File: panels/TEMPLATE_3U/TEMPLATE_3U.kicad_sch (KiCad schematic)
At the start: 6 parts

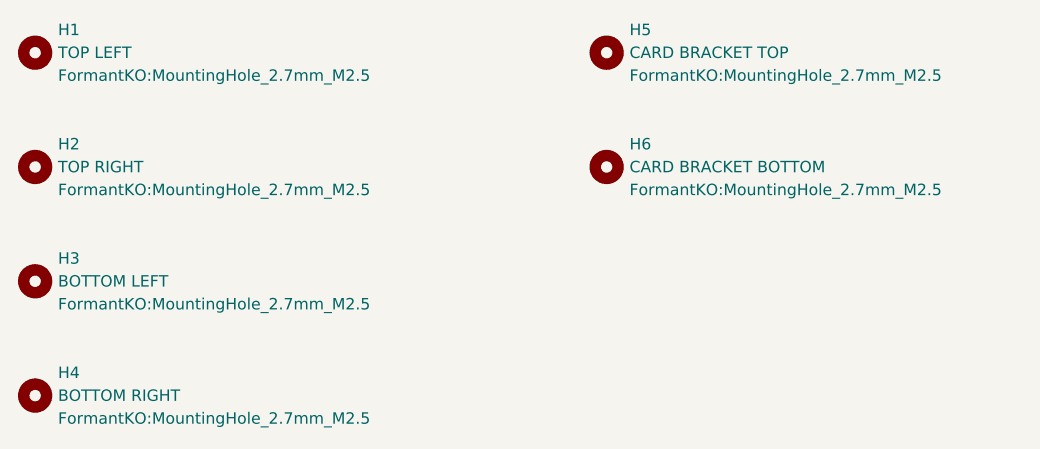
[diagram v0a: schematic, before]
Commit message: panel mounting holes
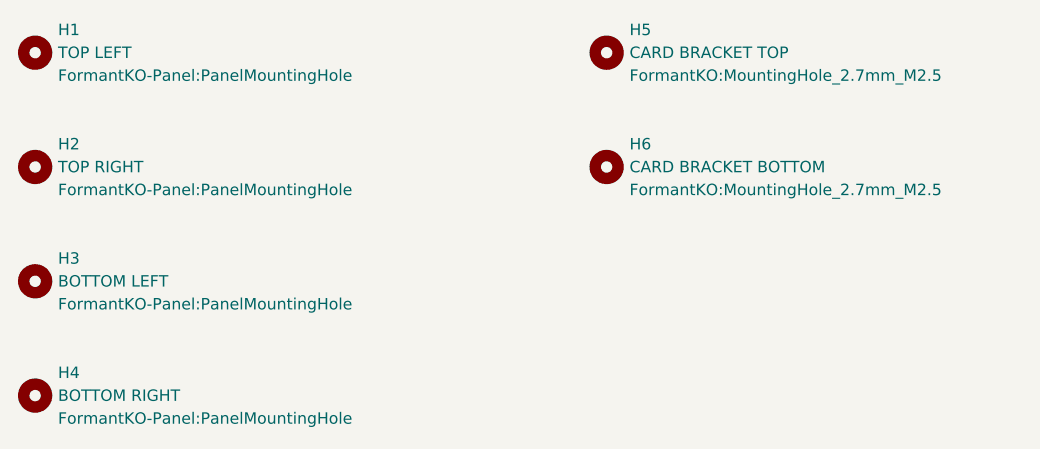
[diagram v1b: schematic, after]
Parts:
- H1, H2, H3, H4: footprint FormantKO:MountingHole_2.7mm_M2.5 -> FormantKO-Panel:PanelMountingHole
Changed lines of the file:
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@@
 			)
 		)
-		(property "Footprint" "FormantKO:MountingHole_2.7mm_M2.5"
+		(property "Footprint" "FormantKO-Panel:PanelMountingHole"
 			(at 53.34 78.7399 0)
 			(show_name no)
@@
 			)
 		)
-		(property "Footprint" "FormantKO:MountingHole_2.7mm_M2.5"
+		(property "Footprint" "FormantKO-Panel:PanelMountingHole"
 			(at 53.34 66.0399 0)
 			(show_name no)
@@
 			)
 		)
-		(property "Footprint" "FormantKO:MountingHole_2.7mm_M2.5"
+		(property "Footprint" "FormantKO-Panel:PanelMountingHole"
 			(at 53.34 53.3399 0)
 			(show_name no)
@@
 			)
 		)
-		(property "Footprint" "FormantKO:MountingHole_2.7mm_M2.5"
+		(property "Footprint" "FormantKO-Panel:PanelMountingHole"
 			(at 53.34 91.4399 0)
 			(show_name no)

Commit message: new adsr, com, vca, and noise panels based on updated template
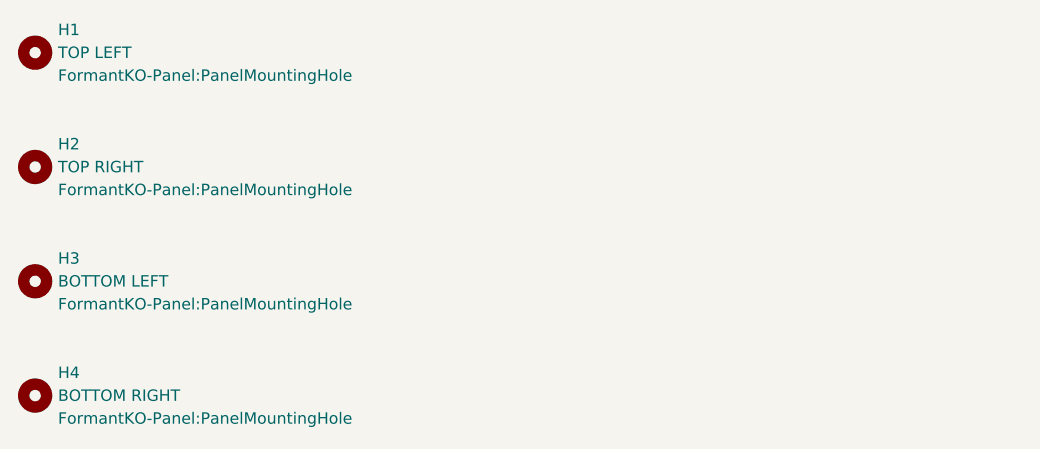
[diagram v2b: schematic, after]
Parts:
- removed H5: CARD BRACKET TOP, FormantKO:MountingHole_2.7mm_M2.5, symbol FormantKO:Mounting_Hole
- removed H6: CARD BRACKET BOTTOM, FormantKO:MountingHole_2.7mm_M2.5, symbol FormantKO:Mounting_Hole
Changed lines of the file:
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@@
-	(symbol
-		(lib_id "FormantKO:Mounting_Hole")
-		(at 114.3 50.8 0)
-		(unit 1)
-		(body_style 1)
-		(exclude_from_sim no)
-		(in_bom no)
-		(on_board yes)
-		(in_pos_files yes)
-		(dnp no)
-		(fields_autoplaced yes)
-		(property "Reference" "H5"
-			(at 116.84 48.2599 0)
-			(show_name no)
-			(do_not_autoplace no)
-			(effects
-				(font
-					(size 1.27 1.27)
-				)
-				(justify left)
-			)
-		)
-		(property "Value" "CARD BRACKET TOP"
-			(at 116.84 50.7999 0)
-			(show_name no)
-			(do_not_autoplace no)
-			(effects
-				(font
-					(size 1.27 1.27)
-				)
-				(justify left)
-			)
-		)
-		(property "Footprint" "FormantKO:MountingHole_2.7mm_M2.5"
-			(at 116.84 53.3399 0)
-			(show_name no)
-			(do_not_autoplace no)
-			(effects
-				(font
-					(size 1.27 1.27)
-				)
-				(justify left)
-			)
-		)
-		(property "Datasheet" ""
-			(at 114.3 50.8 0)
-			(hide yes)
-			(show_name no)
-			(do_not_autoplace no)
-			(effects
-				(font
-					(size 1.27 1.27)
-				)
-			)
-		)
-		(property "Description" "Mounting Hole without connection"
-			(at 114.3 50.8 0)
-			(hide yes)
-			(show_name no)
-			(do_not_autoplace no)
-			(effects
-				(font
-					(size 1.27 1.27)
-				)
-			)
-		)
-		(instances
-			(project "TEMPLATE_3U"
-				(path "/821ca410-94a8-44ad-b9ec-558d50597dcb"
-					(reference "H5")
-					(unit 1)
-				)
-			)
-		)
-	)
 	(symbol
 		(lib_id "FormantKO:Mounting_Hole")
@@
 					(unit 1)
 				)
-			)
-		)
-	)
-	(symbol
-		(lib_id "FormantKO:Mounting_Hole")
-		(at 114.3 63.5 0)
-		(unit 1)
-		(body_style 1)
-		(exclude_from_sim no)
-		(in_bom no)
-		(on_board yes)
-		(in_pos_files yes)
-		(dnp no)
-		(fields_autoplaced yes)
-		(property "Reference" "H6"
-			(at 116.84 60.9599 0)
-			(show_name no)
-			(do_not_autoplace no)
-			(effects
-				(font
-					(size 1.27 1.27)
-				)
-				(justify left)
-			)
-		)
-		(property "Value" "CARD BRACKET BOTTOM"
-			(at 116.84 63.4999 0)
-			(show_name no)
-			(do_not_autoplace no)
-			(effects
-				(font
-					(size 1.27 1.27)
-				)
-				(justify left)
-			)
-		)
-		(property "Footprint" "FormantKO:MountingHole_2.7mm_M2.5"
-			(at 116.84 66.0399 0)
-			(show_name no)
-			(do_not_autoplace no)
-			(effects
-				(font
-					(size 1.27 1.27)
-				)
-				(justify left)
-			)
-		)
-		(property "Datasheet" ""
-			(at 114.3 63.5 0)
-			(hide yes)
-			(show_name no)
-			(do_not_autoplace no)
-			(effects
-				(font
-					(size 1.27 1.27)
-				)
-			)
-		)
-		(property "Description" "Mounting Hole without connection"
-			(at 114.3 63.5 0)
-			(hide yes)
-			(show_name no)
-			(do_not_autoplace no)
-			(effects
-				(font
-					(size 1.27 1.27)
-				)
-			)
-		)
-		(instances
-			(project "TEMPLATE_3U"
-				(path "/821ca410-94a8-44ad-b9ec-558d50597dcb"
-					(reference "H6")
-					(unit 1)
-				)
